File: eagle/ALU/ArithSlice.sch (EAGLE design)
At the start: 0 parts

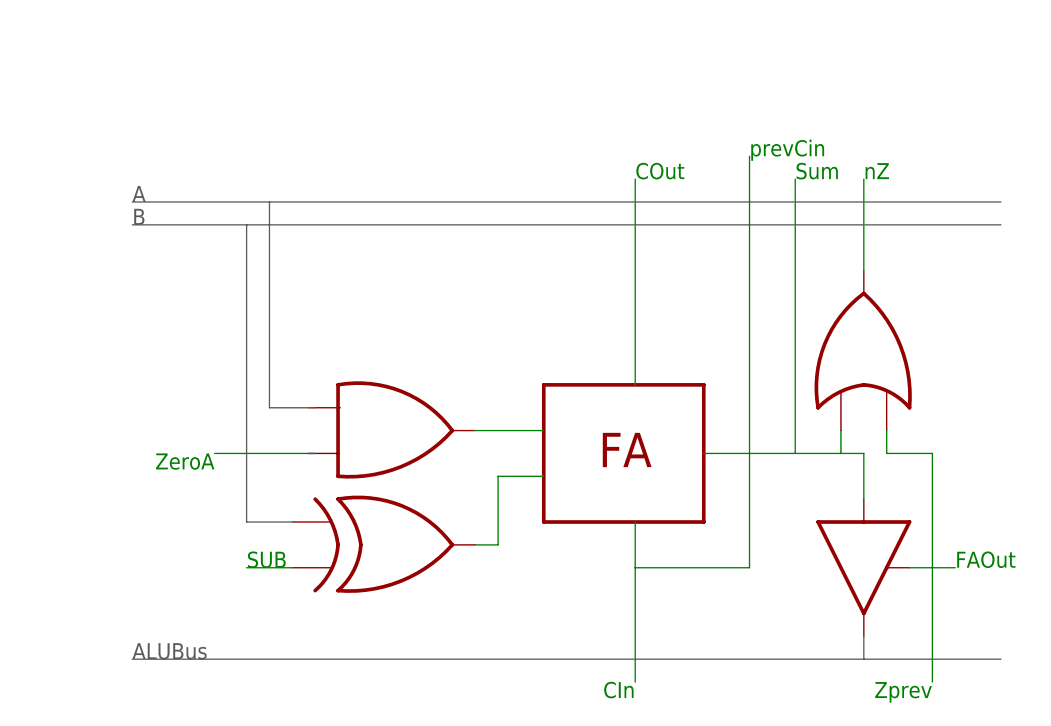
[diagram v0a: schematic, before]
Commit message: FR:ALU design reduction and rewording
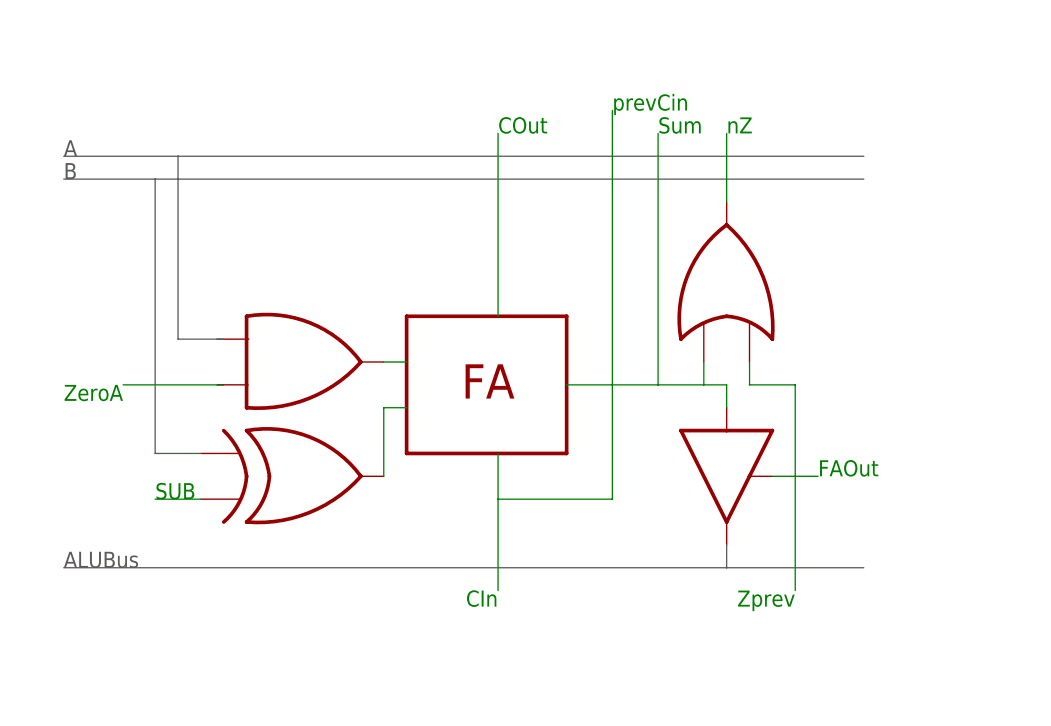
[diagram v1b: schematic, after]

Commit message: Eagle schematics now use library
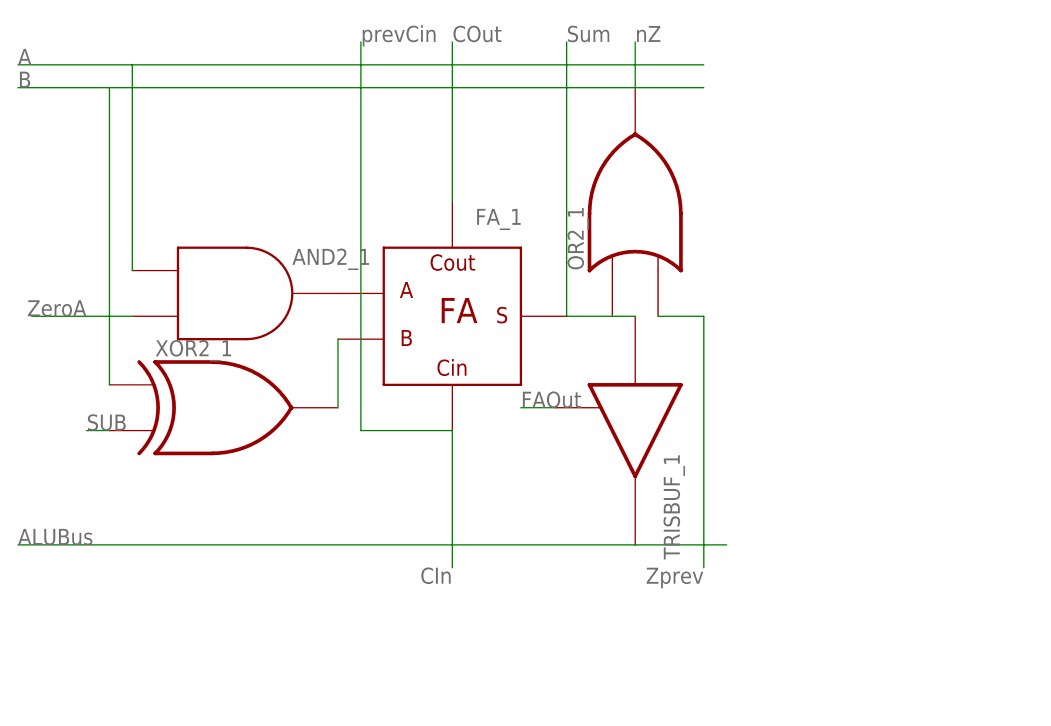
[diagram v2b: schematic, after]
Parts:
- added AND2_1: AND2, c035u:AND2
- added FA_1: FULLADDER, c035u:FULLADDER
- added OR2_1: OR2, c035u:OR2
- added TRISBUF_1: TRISBUF, c035u:TRISBUF
- added XOR2_1: XOR2, c035u:XOR2
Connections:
- new net N$13: AND2_1.O, FA_1.A
- new net N$14: FA_1.B, XOR2_1.O
- new net N$15: XOR2_1.I1
- new net N$16: FA_1.COUT
- new net N$17: TRISBUF_1.P$1
- new net N$18: FA_1.S, OR2_1.I0, TRISBUF_1.I
- new net N$19: OR2_1.I1
- new net N$20: OR2_1.O
- new net N$22: TRISBUF_1.O
- new net N$23: XOR2_1.I0
- new net N$24: AND2_1.A
- new net N$25: FA_1.CIN
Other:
- note removed: "FA"

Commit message: Schematics small improvements
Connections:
- removed net N$22: TRISBUF_1.O
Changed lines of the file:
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@@
 </instances>
 <busses>
+<bus name="B$1">
+<segment>
+<wire x1="-20.32" y1="86.36" x2="58.42" y2="86.36" width="0.1524" layer="92"/>
+</segment>
+</bus>
 </busses>
 <nets>
@@
 <wire x1="48.26" y1="111.76" x2="45.72" y2="111.76" width="0.1524" layer="91"/>
 <wire x1="40.64" y1="111.76" x2="45.72" y2="111.76" width="0.1524" layer="91"/>
+<junction x="45.72" y="111.76"/>
+<junction x="40.64" y="111.76"/>
 </segment>
 </net>
@@
 <pinref part="XOR2_1" gate="G$1" pin="I0"/>
 <wire x1="-10.16" y1="104.14" x2="-10.16" y2="137.16" width="0.1524" layer="91"/>
+<wire x1="-20.32" y1="137.16" x2="-10.16" y2="137.16" width="0.1524" layer="91"/>
+<junction x="-10.16" y="137.16"/>
+<wire x1="-10.16" y1="137.16" x2="55.88" y2="137.16" width="0.1524" layer="91"/>
 </segment>
 </net>
@@
 <pinref part="AND2_1" gate="G$1" pin="A"/>
 <wire x1="-7.62" y1="116.84" x2="-7.62" y2="139.7" width="0.1524" layer="91"/>
+<wire x1="-20.32" y1="139.7" x2="-7.62" y2="139.7" width="0.1524" layer="91"/>
+<junction x="-7.62" y="139.7"/>
+<wire x1="-7.62" y1="139.7" x2="55.88" y2="139.7" width="0.1524" layer="91"/>
 </segment>
 </net>
@@
 <wire x1="27.94" y1="99.06" x2="17.78" y2="99.06" width="0.1524" layer="91"/>
 <wire x1="17.78" y1="99.06" x2="17.78" y2="142.24" width="0.1524" layer="91"/>
+<junction x="27.94" y="99.06"/>
 </segment>
 </net>
@@
 </segment>
 </net>
-<net name="N$22" class="0">
-<segment>
-<wire x1="-20.32" y1="86.36" x2="48.26" y2="86.36" width="0.1524" layer="91"/>
-<pinref part="TRISBUF_1" gate="G$1" pin="O"/>
-<wire x1="48.26" y1="86.36" x2="58.42" y2="86.36" width="0.1524" layer="91"/>
-</segment>
-</net>
-<net name="N$26" class="0">
-<segment>
-<wire x1="-20.32" y1="137.16" x2="55.88" y2="137.16" width="0.1524" layer="91"/>
-</segment>
-</net>
-<net name="N$27" class="0">
-<segment>
-<wire x1="-20.32" y1="139.7" x2="55.88" y2="139.7" width="0.1524" layer="91"/>
-</segment>
-</net>
